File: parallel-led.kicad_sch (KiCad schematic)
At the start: 11 parts

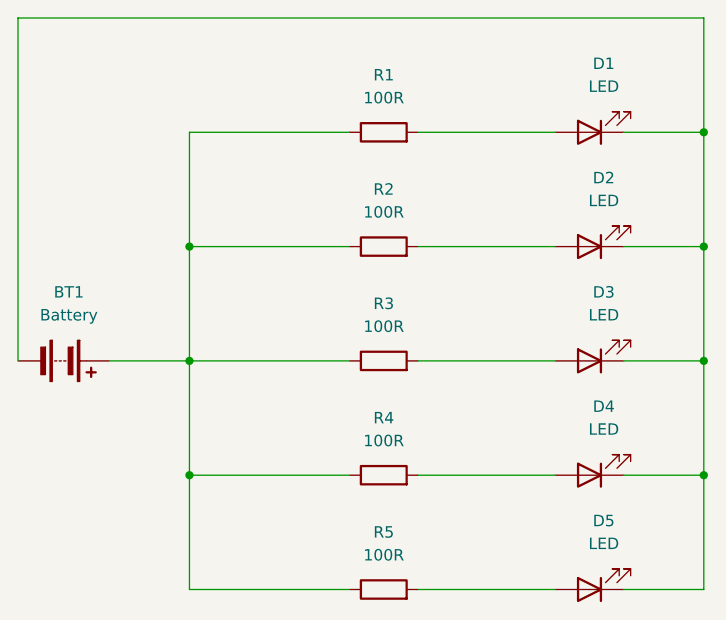
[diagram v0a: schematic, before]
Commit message: fix components' footprint
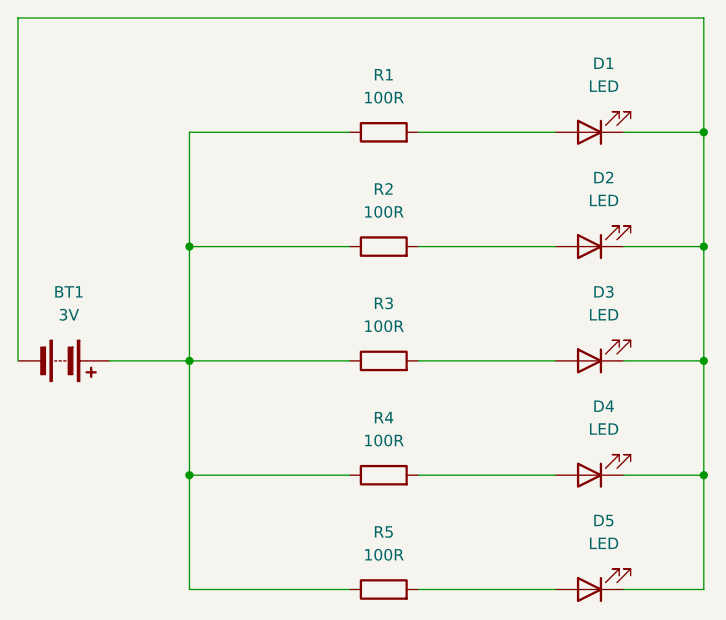
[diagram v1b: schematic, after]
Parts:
- BT1: value Battery -> 3V; footprint (none) -> Battery:BatteryHolder_Keystone_2462_2xAA
- D1, D2, D3, D4, D5: footprint (none) -> LED_THT:LED_D5.0mm
- R1, R2, R3, R4, R5: footprint (none) -> Resistor_THT:R_Axial_DIN0207_L6.3mm_D2.5mm_P7.62mm_Horizontal

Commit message: refining pcb design
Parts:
- BT1: footprint Battery:BatteryHolder_Keystone_2462_2xAA -> TerminalBlock:TerminalBlock_Altech_AK300-2_P5.00mm
- R1, R2, R3, R4, R5: footprint Resistor_THT:R_Axial_DIN0207_L6.3mm_D2.5mm_P7.62mm_Horizontal -> Resistor_THT:R_Axial_DIN0207_L6.3mm_D2.5mm_P10.16mm_Horizontal
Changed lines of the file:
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@@
+    (stroke (width 0) (type default))
+  )
+  (wire (pts (xy 104.14 101.6) (xy 107.95 101.6))
     (stroke (width 0) (type default))
   )
@@
     (stroke (width 0) (type default))
   )
-  (wire (pts (xy 165.1 63.5) (xy 88.9 63.5))
+  (wire (pts (xy 165.1 63.5) (xy 93.98 63.5))
     (stroke (width 0) (type default))
   )
@@
     (stroke (width 0) (type default))
   )
+  (wire (pts (xy 107.95 88.9) (xy 107.95 76.2))
+    (stroke (width 0) (type default))
+  )
+  (wire (pts (xy 107.95 101.6) (xy 107.95 114.3))
+    (stroke (width 0) (type default))
+  )
+  (wire (pts (xy 133.35 114.3) (xy 148.59 114.3))
+    (stroke (width 0) (type default))
+  )
+  (wire (pts (xy 107.95 114.3) (xy 107.95 127))
+    (stroke (width 0) (type default))
+  )
+  (wire (pts (xy 156.21 114.3) (xy 165.1 114.3))
+    (stroke (width 0) (type default))
+  )
+  (wire (pts (xy 165.1 114.3) (xy 165.1 101.6))
+    (stroke (width 0) (type default))
+  )
+  (wire (pts (xy 107.95 88.9) (xy 125.73 88.9))
+    (stroke (width 0) (type default))
+  )
+  (wire (pts (xy 156.21 88.9) (xy 165.1 88.9))
+    (stroke (width 0) (type default))
+  )
+  (wire (pts (xy 165.1 127) (xy 165.1 114.3))
+    (stroke (width 0) (type default))
+  )
+  (wire (pts (xy 165.1 101.6) (xy 165.1 88.9))
+    (stroke (width 0) (type default))
+  )
+  (wire (pts (xy 133.35 127) (xy 148.59 127))
+    (stroke (width 0) (type default))
+  )
+  (wire (pts (xy 93.98 63.5) (xy 93.98 101.6))
+    (stroke (width 0) (type default))
+  )
   (wire (pts (xy 107.95 101.6) (xy 125.73 101.6))
     (stroke (width 0) (type default))
   )
-  (wire (pts (xy 107.95 88.9) (xy 107.95 76.2))
-    (stroke (width 0) (type default))
-  )
-  (wire (pts (xy 99.06 101.6) (xy 107.95 101.6))
-    (stroke (width 0) (type default))
-  )
-  (wire (pts (xy 133.35 114.3) (xy 148.59 114.3))
-    (stroke (width 0) (type default))
-  )
-  (wire (pts (xy 107.95 114.3) (xy 107.95 127))
-    (stroke (width 0) (type default))
-  )
-  (wire (pts (xy 88.9 63.5) (xy 88.9 101.6))
-    (stroke (width 0) (type default))
-  )
-  (wire (pts (xy 156.21 114.3) (xy 165.1 114.3))
-    (stroke (width 0) (type default))
-  )
-  (wire (pts (xy 165.1 114.3) (xy 165.1 101.6))
-    (stroke (width 0) (type default))
-  )
-  (wire (pts (xy 107.95 88.9) (xy 125.73 88.9))
-    (stroke (width 0) (type default))
-  )
-  (wire (pts (xy 156.21 88.9) (xy 165.1 88.9))
-    (stroke (width 0) (type default))
-  )
-  (wire (pts (xy 165.1 127) (xy 165.1 114.3))
-    (stroke (width 0) (type default))
-  )
-  (wire (pts (xy 165.1 101.6) (xy 165.1 88.9))
-    (stroke (width 0) (type default))
-  )
-  (wire (pts (xy 133.35 127) (xy 148.59 127))
-    (stroke (width 0) (type default))
-  )
-  (wire (pts (xy 107.95 101.6) (xy 107.95 114.3))
-    (stroke (width 0) (type default))
-  )
   (wire (pts (xy 107.95 127) (xy 125.73 127))
     (stroke (width 0) (type default))
   )
+  (symbol (lib_id "Device:Battery") (at 99.06 101.6 270) (unit 1)
+    (in_bom yes) (on_board yes) (dnp no) (fields_autoplaced)
+    (property "Reference" "BT1" (at 99.6315 93.98 90)
+      (effects (font (size 1.27 1.27)))
+    )
+    (property "Value" "3V" (at 99.6315 96.52 90)
+      (effects (font (size 1.27 1.27)))
+    )
+    (property "Footprint" "TerminalBlock:TerminalBlock_Altech_AK300-2_P5.00mm" (at 100.584 101.6 90)
+      (effects (font (size 1.27 1.27)) hide)
+    )
+    (property "Datasheet" "~" (at 100.584 101.6 90)
+      (effects (font (size 1.27 1.27)) hide)
+    )
+    (pin "1")
+    (pin "2")
+    (instances
+      (project "parallel-led"
+        (path "/0057777c-c240-499d-8256-90336a835359"
+          (reference "BT1") (unit 1)
+        )
+      )
+    )
+  )
   (symbol (lib_id "Device:R") (at 129.54 88.9 90) (unit 1)
     (in_bom yes) (on_board yes) (dnp no) (fields_autoplaced)
@@
       (effects (font (size 1.27 1.27)))
     )
-    (property "Footprint" "Resistor_THT:R_Axial_DIN0207_L6.3mm_D2.5mm_P7.62mm_Horizontal" (at 129.54 90.678 90)
+    (property "Footprint" "Resistor_THT:R_Axial_DIN0207_L6.3mm_D2.5mm_P10.16mm_Horizontal" (at 129.54 90.678 90)
       (effects (font (size 1.27 1.27)) hide)
     )
@@
       (effects (font (size 1.27 1.27)))
     )
-    (property "Footprint" "Resistor_THT:R_Axial_DIN0207_L6.3mm_D2.5mm_P7.62mm_Horizontal" (at 129.54 103.378 90)
+    (property "Footprint" "Resistor_THT:R_Axial_DIN0207_L6.3mm_D2.5mm_P10.16mm_Horizontal" (at 129.54 103.378 90)
       (effects (font (size 1.27 1.27)) hide)
     )
@@
       (effects (font (size 1.27 1.27)))
     )
-    (property "Footprint" "Resistor_THT:R_Axial_DIN0207_L6.3mm_D2.5mm_P7.62mm_Horizontal" (at 129.54 116.078 90)
+    (property "Footprint" "Resistor_THT:R_Axial_DIN0207_L6.3mm_D2.5mm_P10.16mm_Horizontal" (at 129.54 116.078 90)
       (effects (font (size 1.27 1.27)) hide)
     )
@@
     )
   )
-  (symbol (lib_id "Device:Battery") (at 93.98 101.6 270) (unit 1)
-    (in_bom yes) (on_board yes) (dnp no) (fields_autoplaced)
-    (property "Reference" "BT1" (at 94.5515 93.98 90)
-      (effects (font (size 1.27 1.27)))
-    )
-    (property "Value" "3V" (at 94.5515 96.52 90)
-      (effects (font (size 1.27 1.27)))
-    )
-    (property "Footprint" "Battery:BatteryHolder_Keystone_2462_2xAA" (at 95.504 101.6 90)
-      (effects (font (size 1.27 1.27)) hide)
-    )
-    (property "Datasheet" "~" (at 95.504 101.6 90)
-      (effects (font (size 1.27 1.27)) hide)
-    )
-    (pin "1")
-    (pin "2")
-    (instances
-      (project "parallel-led"
-        (path "/0057777c-c240-499d-8256-90336a835359"
-          (reference "BT1") (unit 1)
-        )
-      )
-    )
-  )
   (symbol (lib_id "Device:R") (at 129.54 127 90) (unit 1)
     (in_bom yes) (on_board yes) (dnp no) (fields_autoplaced)
@@
       (effects (font (size 1.27 1.27)))
     )
-    (property "Footprint" "Resistor_THT:R_Axial_DIN0207_L6.3mm_D2.5mm_P7.62mm_Horizontal" (at 129.54 128.778 90)
+    (property "Footprint" "Resistor_THT:R_Axial_DIN0207_L6.3mm_D2.5mm_P10.16mm_Horizontal" (at 129.54 128.778 90)
       (effects (font (size 1.27 1.27)) hide)
     )
@@
       (effects (font (size 1.27 1.27)))
     )
-    (property "Footprint" "Resistor_THT:R_Axial_DIN0207_L6.3mm_D2.5mm_P7.62mm_Horizontal" (at 129.54 77.978 90)
-      (effects (font (size 1.27 1.27)) hide)
-    )
+    (property "Footprint" "Resistor_THT:R_Axial_DIN0207_L6.3mm_D2.5mm_P10.16mm_Horizontal" (at 129.54 77.978 90)
+      (effects (font (size 1.27 1.27)) hide)
+    )

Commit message: replace led with custom footprint
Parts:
- D1, D2, D3, D4, D5: footprint LED_THT:LED_D5.0mm -> BeginnerModules:BeginnerLED_D5.0mm
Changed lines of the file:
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@@
       (effects (font (size 1.27 1.27)))
     )
-    (property "Footprint" "LED_THT:LED_D5.0mm" (at 152.4 127 0)
+    (property "Footprint" "BeginnerModules:BeginnerLED_D5.0mm" (at 152.4 127 0)
       (effects (font (size 1.27 1.27)) hide)
     )
@@
       (effects (font (size 1.27 1.27)))
     )
-    (property "Footprint" "LED_THT:LED_D5.0mm" (at 152.4 101.6 0)
+    (property "Footprint" "BeginnerModules:BeginnerLED_D5.0mm" (at 152.4 101.6 0)
       (effects (font (size 1.27 1.27)) hide)
     )
@@
       (effects (font (size 1.27 1.27)))
     )
-    (property "Footprint" "LED_THT:LED_D5.0mm" (at 152.4 88.9 0)
+    (property "Footprint" "BeginnerModules:BeginnerLED_D5.0mm" (at 152.4 88.9 0)
       (effects (font (size 1.27 1.27)) hide)
     )
@@
       (effects (font (size 1.27 1.27)))
     )
-    (property "Footprint" "LED_THT:LED_D5.0mm" (at 152.4 76.2 0)
+    (property "Footprint" "BeginnerModules:BeginnerLED_D5.0mm" (at 152.4 76.2 0)
       (effects (font (size 1.27 1.27)) hide)
     )
@@
       (effects (font (size 1.27 1.27)))
     )
-    (property "Footprint" "LED_THT:LED_D5.0mm" (at 152.4 114.3 0)
+    (property "Footprint" "BeginnerModules:BeginnerLED_D5.0mm" (at 152.4 114.3 0)
       (effects (font (size 1.27 1.27)) hide)
     )
